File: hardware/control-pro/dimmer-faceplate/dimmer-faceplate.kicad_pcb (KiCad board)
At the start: 2 copper layers, 100 x 90 mm, 14 parts

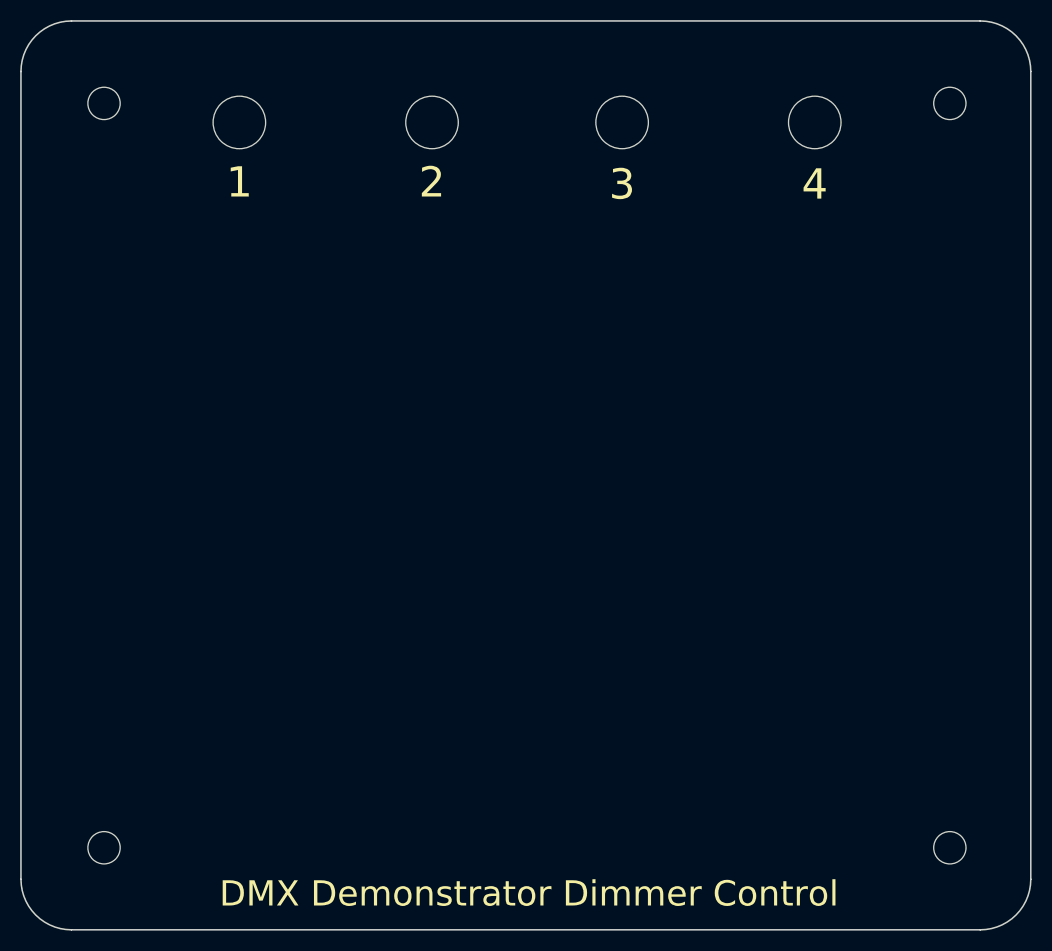
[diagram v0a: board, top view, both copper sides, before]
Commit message: Add copper pours to faceplates.
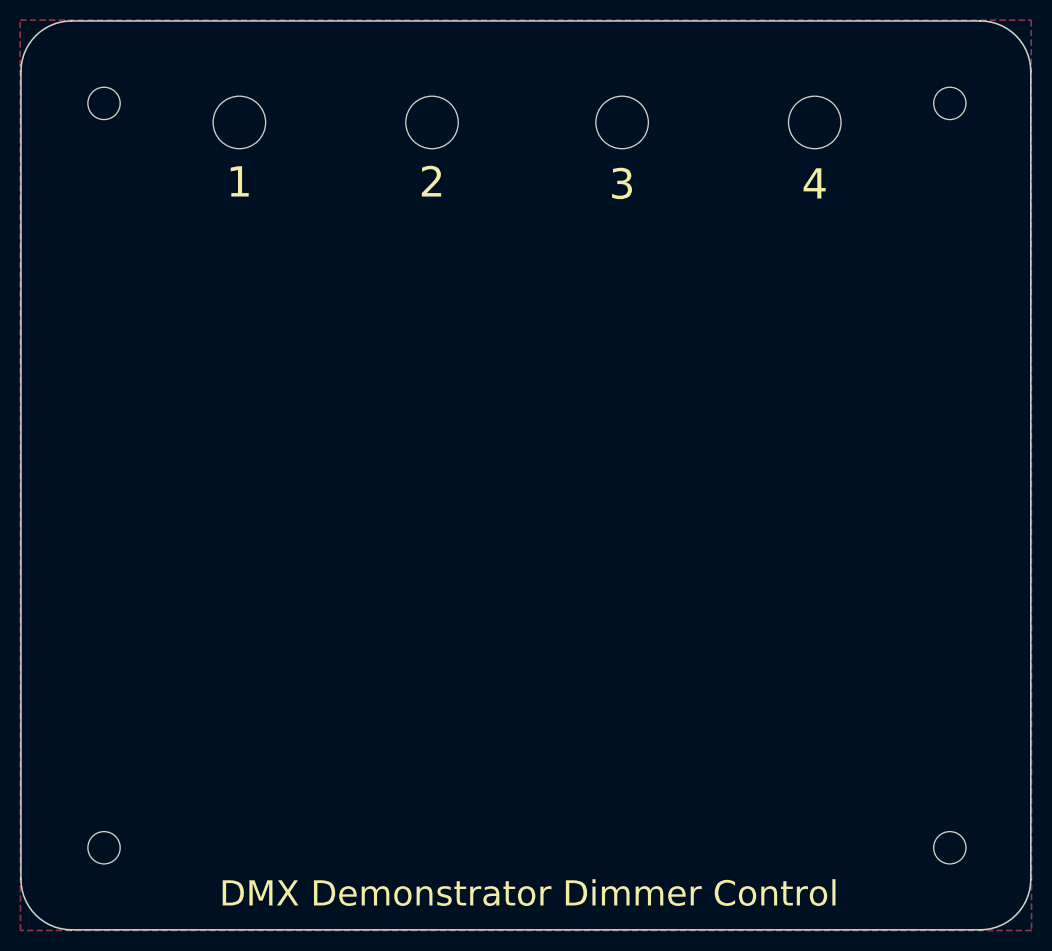
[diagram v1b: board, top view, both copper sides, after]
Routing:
- added copper zone on B.Cu, net (none)
- added copper zone on F.Cu, net (none)
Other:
- board text added: "DMX-CPDF, Rev 1.3 Crazy Giraffe Software"
- board text removed: "DMX-CPDF, Rev 1.2 Crazy Giraffe Software"
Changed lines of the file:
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@@
   (title_block
     (title "DMX Demonstrator - Control-Pro Dimmer (DMX-CPDF)")
-    (date 2023-02-11)
-    (rev 1.2)
+    (date 2023-12-04)
+    (rev 1.3)
     (company "Crazy Giraffe Software")
     (comment 2 "Designed by: SparkyBobo")
@@
     (effects (font (size 2.5 2.5) (thickness 0.45)))
   )
-  (gr_text "DMX-CPDF, Rev 1.2\nCrazy Giraffe Software" (at 160.414 136.102) (layer B.SilkS)
+  (gr_text "DMX-CPDF, Rev 1.3\nCrazy Giraffe Software" (at 160.414 136.102) (layer B.SilkS)
     (effects (font (size 1 1) (thickness 0.15)) (justify mirror))
   )
@@
   (gr_circle (center 179.088 56.804285) (end 179.85 51.216285) (layer Dwgs.User) (width 0.2))
   (gr_circle (center 95.33 56.856) (end 100.969715 56.856) (layer Dwgs.User) (width 0.2))
+  (zone (net 0) (net_name "") (layer F.Cu) (hatch edge 0.508)
+    (connect_pads (clearance 0.508))
+    (min_thickness 0.254)
+    (fill yes (arc_segments 16) (thermal_gap 0.508) (thermal_bridge_width 0.508))
+    (polygon
+      (pts
+        (xy 187.1599 48.63338) (xy 187.17514 138.7602) (xy 87.05596 138.75766) (xy 87.04326 48.62576)
+      )
+    )
+  )
+  (zone (net 0) (net_name "") (layer B.Cu) (hatch edge 0.508)
+    (connect_pads (clearance 0.508))
+    (min_thickness 0.254)
+    (fill yes (arc_segments 16) (thermal_gap 0.508) (thermal_bridge_width 0.508))
+    (polygon
+      (pts
+        (xy 187.1599 48.633182) (xy 187.17514 138.760002) (xy 87.05596 138.757462) (xy 87.04326 48.625562)
+      )
+    )
+  )
 )
